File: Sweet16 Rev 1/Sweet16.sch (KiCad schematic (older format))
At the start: 67 parts, among them J1 Conn_01x09_Male, J10 SW_half_inverter, J11 R_clock, J12 OUT_clock, J13 SW_dual8_hex, J14 OUT_OUT, J15 R_sync_pitch_1, J16 SW_sync_1, J17 R_sync_pitch_2, J18 SW_sync_2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

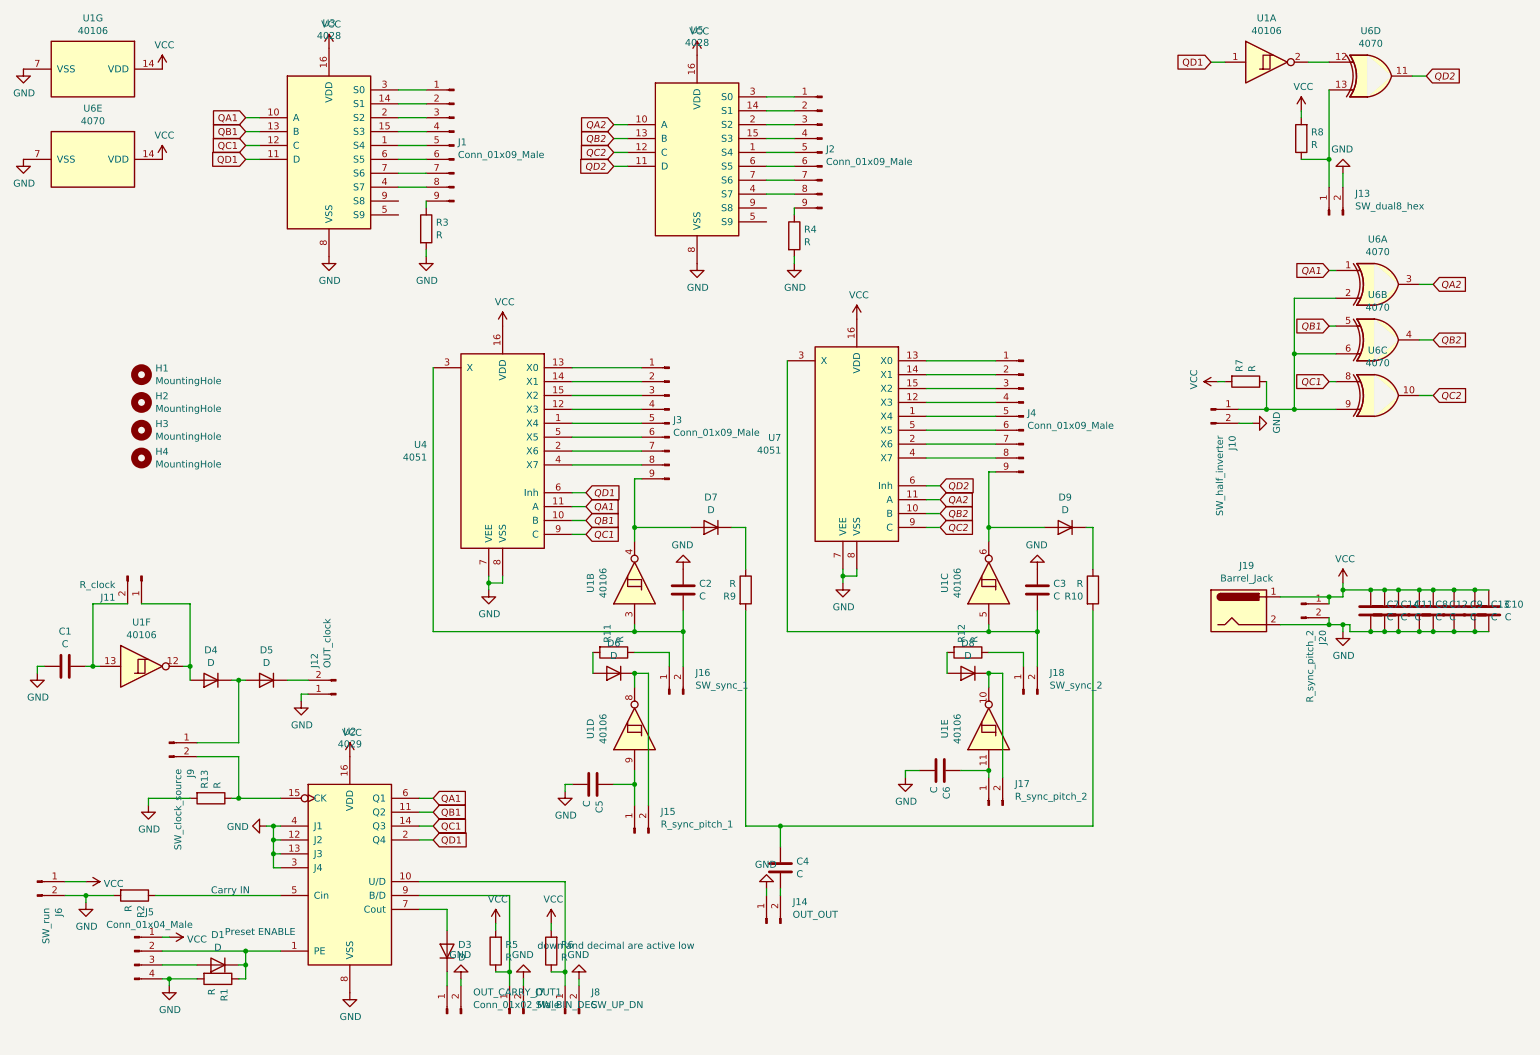
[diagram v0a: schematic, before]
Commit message: moved bits added labels
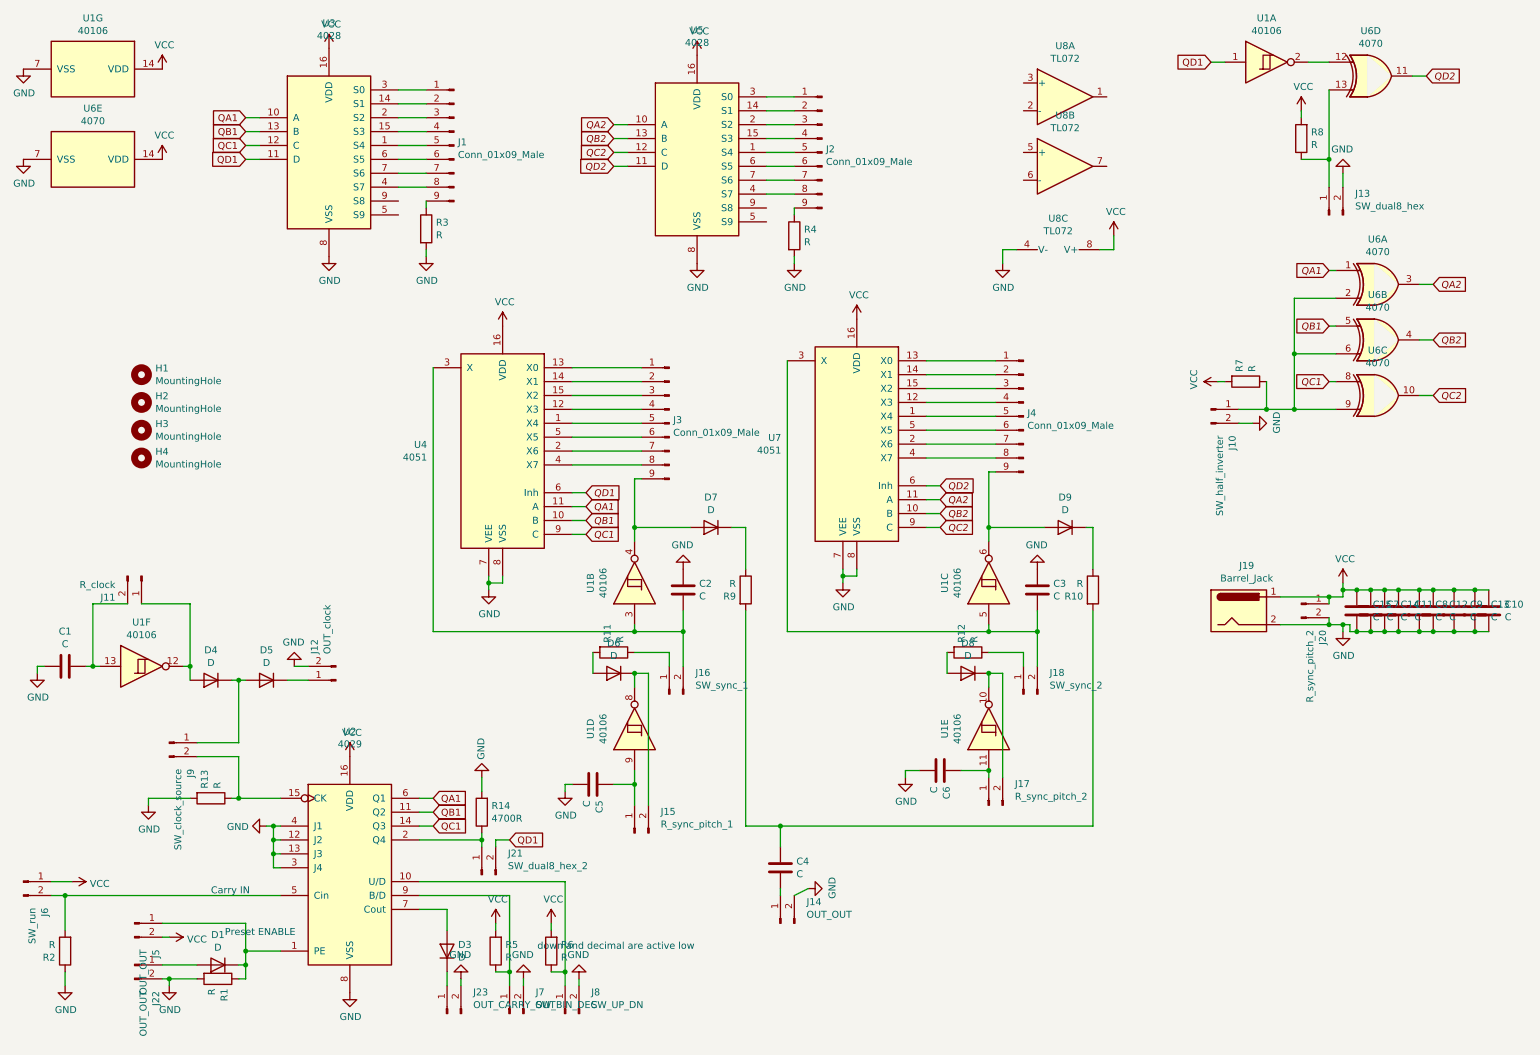
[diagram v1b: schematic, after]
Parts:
- removed J5: Conn_01x04_Male, Connector_PinHeader_2.54mm:PinHeader_1x04_P2.54mm_Vertical, symbol Connector:Conn_01x04_Male
- added C15: C, Capacitor_THT:C_Disc_D6.0mm_W2.5mm_P5.00mm, symbol Device:C
- added J21: SW_dual8_hex_2, Connector_PinHeader_2.54mm:PinHeader_1x02_P2.54mm_Vertical, symbol Connector:Conn_01x02_Male
- added J22, J5: OUT_OUT, Connector_PinHeader_2.54mm:PinHeader_1x02_P2.54mm_Vertical, symbol Connector:Conn_01x02_Male
- added R14: 4700R, Resistor_THT:R_Axial_DIN0207_L6.3mm_D2.5mm_P7.62mm_Horizontal, symbol Device:R
- added U8: TL072, Package_DIP:DIP-8_W7.62mm_LongPads, symbol Amplifier_Operational:TL072
- J23: renamed from OUT_CARRY_OUT1; value Conn_01x02_Male -> OUT_CARRY_OUT
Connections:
- net GND: now also J12.2 (Pin_2), J14.2 (Pin_2), R2.1, C15.1, J22.2 (Pin_2), R14.2, U8.4 (V-); no longer J12.1 (Pin_1), J14.1 (Pin_1), J6.2 (Pin_2), R2.2
- net QD1: now also J21.2 (Pin_2); no longer U2.2 (Q4)
- net VCC: now also C15.2, J5.2 (Pin_2), U8.8 (V+)
- net at D1.1 (K), R1.1, U2.1 (PE): now also J5.1 (Pin_1)
- net at U2.5 (Cin): now also J6.2 (Pin_2), R2.2; no longer R2.1
- net at D1.2 (A): now also J22.1 (Pin_1)
- net at D5.1 (K): now also J12.1 (Pin_1); no longer J12.2 (Pin_2)
- net at C4.1: now also J14.1 (Pin_1); no longer J14.2 (Pin_2)
- new net: J21.1 (Pin_1), R14.1, U2.2 (Q4)
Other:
- moved on the sheet: J12, J14, J6, R2

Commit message: labels
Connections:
- net at D6.1 (K), U1.8: now also J15.1 (Pin_1); no longer J15.2 (Pin_2)
- net at C5.2, U1.9: now also J15.2 (Pin_2); no longer J15.1 (Pin_1)
- net at D8.1 (K), U1.10: now also J17.1 (Pin_1); no longer J17.2 (Pin_2)
- net at C6.2, U1.11: now also J17.2 (Pin_2); no longer J17.1 (Pin_1)
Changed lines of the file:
@@
 L Connector:Conn_01x02_Male J15
 U 1 1 5FCE153F
-P 5000 6400
-F 0 "J15" V 5154 6212 50  0000 R CNN
-F 1 "R_sync_pitch_1" V 5063 6212 50  0000 R CNN
-F 2 "Connector_PinHeader_2.54mm:PinHeader_1x02_P2.54mm_Vertical" H 5000 6400 50  0001 C CNN
-F 3 "~" H 5000 6400 50  0001 C CNN
-	1    5000 6400
-	0    -1   -1   0
+P 5100 6400
+F 0 "J15" V 5254 6212 50  0000 R CNN
+F 1 "R_sync_pitch_1" V 5163 6212 50  0000 R CNN
+F 2 "Connector_PinHeader_2.54mm:PinHeader_1x02_P2.54mm_Vertical" H 5100 6400 50  0001 C CNN
+F 3 "~" H 5100 6400 50  0001 C CNN
+	1    5100 6400
+	0    1    -1   0
 $EndComp
 $Comp
@@
 L Connector:Conn_01x02_Male J17
 U 1 1 5FCDFDEC
-P 7550 6200
-F 0 "J17" V 7704 6012 50  0000 R CNN
-F 1 "R_sync_pitch_2" V 7613 6012 50  0000 R CNN
-F 2 "Connector_PinHeader_2.54mm:PinHeader_1x02_P2.54mm_Vertical" H 7550 6200 50  0001 C CNN
-F 3 "~" H 7550 6200 50  0001 C CNN
-	1    7550 6200
-	0    -1   -1   0
+P 7650 6200
+F 0 "J17" V 7804 6012 50  0000 R CNN
+F 1 "R_sync_pitch_2" V 7713 6012 50  0000 R CNN
+F 2 "Connector_PinHeader_2.54mm:PinHeader_1x02_P2.54mm_Vertical" H 7650 6200 50  0001 C CNN
+F 3 "~" H 7650 6200 50  0001 C CNN
+	1    7650 6200
+	0    1    -1   0
 $EndComp
 $Comp
@@
 	10200 4650 10100 4650
 $Comp
-L power:GND #PWR?
+L power:GND #PWR0142
 U 1 1 6154B30B
 P 7650 2300
-F 0 "#PWR?" H 7650 2050 50  0001 C CNN
+F 0 "#PWR0142" H 7650 2050 50  0001 C CNN
 F 1 "GND" H 7655 2127 50  0000 C CNN
 F 2 "" H 7650 2300 50  0001 C CNN
@@
 $EndComp
 $Comp
-L power:VCC #PWR?
+L power:VCC #PWR0143
 U 1 1 6154BF9B
 P 8450 2100
-F 0 "#PWR?" H 8450 1950 50  0001 C CNN
+F 0 "#PWR0143" H 8450 1950 50  0001 C CNN
 F 1 "VCC" H 8465 2273 50  0000 C CNN
 F 2 "" H 8450 2100 50  0001 C CNN

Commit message: 48 wires to go
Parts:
- removed D7, D9: D, Diode_THT:D_A-405_P7.62mm_Horizontal, symbol Device:D
- removed J19: Barrel_Jack, Connector_BarrelJack:BarrelJack_CUI_PJ-102AH_Horizontal, symbol Connector:Barrel_Jack
- removed R10, R9: R, Resistor_THT:R_Axial_DIN0207_L6.3mm_D2.5mm_P7.62mm_Horizontal, symbol Device:R
- removed U8: TL072, Package_DIP:DIP-8_W7.62mm_LongPads, symbol Amplifier_Operational:TL072
- added R15, R16: 100k, Resistor_THT:R_Axial_DIN0207_L6.3mm_D2.5mm_P7.62mm_Horizontal, symbol Device:R
- added U8: LM358, Package_DIP:DIP-8_W7.62mm_LongPads, symbol Amplifier_Operational:LM358
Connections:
- net GND: now also U8.4 (V-)
- net VCC: now also U8.8 (V+)
- net at J3.9 (Pin_9), U1.4: now also U8.5 (+)
- net at J4.9 (Pin_9), U1.6: now also U8.3 (+)
- net at C4.2: now also R15.1, R16.2
- new net: R16.1, U8.1, U8.2 (-)
- new net: R15.2, U8.6 (-), U8.7
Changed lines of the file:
@@
 	7550 4200 7550 4300
-$Comp
-L Device:R R9
-U 1 1 600316E2
-P 5800 4650
-F 0 "R9" H 5730 4604 50  0000 R CNN
-F 1 "R" H 5730 4695 50  0000 R CNN
-F 2 "Resistor_THT:R_Axial_DIN0207_L6.3mm_D2.5mm_P7.62mm_Horizontal" V 5730 4650 50  0001 C CNN
-F 3 "~" H 5800 4650 50  0001 C CNN
-	1    5800 4650
-	1    0    0    -1
-$EndComp
 $Comp
 L Connector:Conn_01x02_Male J10
@@
 	9550 3350 9750 3350
 $Comp
-L Device:R R10
-U 1 1 60329897
-P 8300 4650
-F 0 "R10" H 8230 4604 50  0000 R CNN
-F 1 "R" H 8230 4695 50  0000 R CNN
-F 2 "Resistor_THT:R_Axial_DIN0207_L6.3mm_D2.5mm_P7.62mm_Horizontal" V 8230 4650 50  0001 C CNN
-F 3 "~" H 8300 4650 50  0001 C CNN
-	1    8300 4650
-	1    0    0    -1
-$EndComp
-Wire Wire Line
-	5800 4800 5800 6350
-Wire Wire Line
-	8300 6350 8300 4800
-Wire Wire Line
-	5800 4200 5800 4500
-Wire Wire Line
-	8300 4200 8300 4500
-$Comp
 L Device:C C4
 U 1 1 603E27DA
@@
 $EndComp
 $Comp
-L Device:D D9
-U 1 1 5FD09EF1
-P 8100 4200
-F 0 "D9" H 8100 3983 50  0000 C CNN
-F 1 "D" H 8100 4074 50  0000 C CNN
-F 2 "Diode_THT:D_A-405_P7.62mm_Horizontal" H 8100 4200 50  0001 C CNN
-F 3 "~" H 8100 4200 50  0001 C CNN
-	1    8100 4200
-	-1   0    0    1
-$EndComp
-$Comp
-L Device:D D7
-U 1 1 5FD0D58A
-P 5550 4200
-F 0 "D7" H 5550 3983 50  0000 C CNN
-F 1 "D" H 5550 4074 50  0000 C CNN
-F 2 "Diode_THT:D_A-405_P7.62mm_Horizontal" H 5550 4200 50  0001 C CNN
-F 3 "~" H 5550 4200 50  0001 C CNN
-	1    5550 4200
-	-1   0    0    1
-$EndComp
-Wire Wire Line
-	5700 4200 5800 4200
-Wire Wire Line
-	8300 4200 8250 4200
-$Comp
 L Device:D D6
 U 1 1 5FD3EE69
@@
 	-1   0    0    1
 $EndComp
-Wire Wire Line
-	6050 6350 8300 6350
-Connection ~ 6050 6350
-Wire Wire Line
-	6050 6350 6050 6500
-Wire Wire Line
-	5800 6350 6050 6350
 $Comp
 L Connector:Conn_01x02_Male J14
@@
 $EndComp
 $Comp
-L Connector:Barrel_Jack J19
-U 1 1 600C4E4A
-P 9350 4800
-F 0 "J19" H 9407 5125 50  0000 C CNN
-F 1 "Barrel_Jack" H 9407 5034 50  0000 C CNN
-F 2 "Connector_BarrelJack:BarrelJack_CUI_PJ-102AH_Horizontal" H 9400 4760 50  0001 C CNN
-F 3 "~" H 9400 4760 50  0001 C CNN
-	1    9350 4800
-	1    0    0    -1
-$EndComp
-$Comp
 L Connector:Conn_01x02_Male J20
 U 1 1 600C58B1
@@
 $EndComp
 Wire Wire Line
-	9650 4700 10000 4700
-Wire Wire Line
 	10100 4700 10100 4650
 Wire Wire Line
@@
 	10100 4650 10100 4600
 Wire Wire Line
-	9650 4900 10000 4900
-Wire Wire Line
 	10100 4900 10100 4950
 Wire Wire Line
@@
 Wire Wire Line
 	10000 4850 10000 4900
-Connection ~ 10000 4900
 Wire Wire Line
 	10000 4900 10100 4900
 Wire Wire Line
 	10000 4750 10000 4700
-Connection ~ 10000 4700
 Wire Wire Line
 	10000 4700 10100 4700
@@
 Wire Wire Line
 	10400 4650 10500 4650
-Wire Wire Line
-	5000 4200 5400 4200
 $Comp
 L power:GND #PWR0138
@@
 	-1   0    0    1
 $EndComp
-Wire Wire Line
-	7550 4200 7950 4200
 $Comp
 L power:GND #PWR0139
@@
 	1600 7050 2200 7050
 $Comp
-L Amplifier_Operational:TL072 U8
-U 1 1 61535B29
-P 8100 1100
-F 0 "U8" H 8100 1467 50  0000 C CNN
-F 1 "TL072" H 8100 1376 50  0000 C CNN
-F 2 "Package_DIP:DIP-8_W7.62mm_LongPads" H 8100 1100 50  0001 C CNN
-F 3 "http://www.ti.com/lit/ds/symlink/tl071.pdf" H 8100 1100 50  0001 C CNN
-	1    8100 1100
-	1    0    0    -1
-$EndComp
-$Comp
-L Amplifier_Operational:TL072 U8
-U 2 1 61536DC3
-P 8100 1600
-F 0 "U8" H 8100 1967 50  0000 C CNN
-F 1 "TL072" H 8100 1876 50  0000 C CNN
-F 2 "Package_DIP:DIP-8_W7.62mm_LongPads" H 8100 1600 50  0001 C CNN
-F 3 "http://www.ti.com/lit/ds/symlink/tl071.pdf" H 8100 1600 50  0001 C CNN
-	2    8100 1600
-	1    0    0    -1
-$EndComp
-$Comp
-L Amplifier_Operational:TL072 U8
-U 3 1 6153A199
-P 8050 2300
-F 0 "U8" V 7725 2300 50  0000 C CNN
-F 1 "TL072" V 7816 2300 50  0000 C CNN
-F 2 "Package_DIP:DIP-8_W7.62mm_LongPads" H 8050 2300 50  0001 C CNN
-F 3 "http://www.ti.com/lit/ds/symlink/tl071.pdf" H 8050 2300 50  0001 C CNN
-	3    8050 2300
-	0    1    1    0
-$EndComp
-$Comp
 L Device:C C15
 U 1 1 6153CD4F
@@
 L power:GND #PWR0142
 U 1 1 6154B30B
-P 7650 2300
-F 0 "#PWR0142" H 7650 2050 50  0001 C CNN
-F 1 "GND" H 7655 2127 50  0000 C CNN
-F 2 "" H 7650 2300 50  0001 C CNN
-F 3 "" H 7650 2300 50  0001 C CNN
-	1    7650 2300
+P 9750 6150
+F 0 "#PWR0142" H 9750 5900 50  0001 C CNN
+F 1 "GND" H 9755 5977 50  0000 C CNN
+F 2 "" H 9750 6150 50  0001 C CNN
+F 3 "" H 9750 6150 50  0001 C CNN
+	1    9750 6150
 	1    0    0    -1
 $EndComp
@@
 L power:VCC #PWR0143
 U 1 1 6154BF9B
-P 8450 2100
-F 0 "#PWR0143" H 8450 1950 50  0001 C CNN
-F 1 "VCC" H 8465 2273 50  0000 C CNN
-F 2 "" H 8450 2100 50  0001 C CNN
-F 3 "" H 8450 2100 50  0001 C CNN
-	1    8450 2100
-	1    0    0    -1
-$EndComp
-Wire Wire Line
-	8350 2200 8450 2200
-Wire Wire Line
-	8450 2200 8450 2100
-Wire Wire Line
-	7750 2200 7650 2200
-Wire Wire Line
-	7650 2200 7650 2300
+P 10550 5950
+F 0 "#PWR0143" H 10550 5800 50  0001 C CNN
+F 1 "VCC" H 10565 6123 50  0000 C CNN
+F 2 "" H 10550 5950 50  0001 C CNN
+F 3 "" H 10550 5950 50  0001 C CNN
+	1    10550 5950
+	1    0    0    -1
+$EndComp
+Wire Wire Line
+	10450 6050 10550 6050
+Wire Wire Line
+	10550 6050 10550 5950
+Wire Wire Line
+	9850 6050 9750 6050
+Wire Wire Line
+	9750 6050 9750 6150
+Wire Wire Line
+	5600 5550 5450 5550
+Wire Wire Line
+	5450 5550 5450 6150
+Wire Wire Line
+	5450 6150 5550 6150
+Wire Wire Line
+	8100 5550 8100 5600
+Wire Wire Line
+	8100 5550 7950 5550
+Wire Wire Line
+	7950 5550 7950 6200
+Wire Wire Line
+	7950 6200 8050 6200
+$Comp
+L Amplifier_Operational:LM358 U8
+U 1 1 6112DB96
+P 8200 5900
+F 0 "U8" V 8154 6130 50  0000 L CNN
+F 1 "LM358" V 8245 6130 50  0000 L CNN
+F 2 "Package_DIP:DIP-8_W7.62mm_LongPads" H 8200 5900 50  0001 C CNN
+F 3 "http://www.ti.com/lit/ds/symlink/lm2904-n.pdf" H 8200 5900 50  0001 C CNN
+	1    8200 5900
+	0    1    1    0
+$EndComp
+$Comp
+L Amplifier_Operational:LM358 U8
+U 2 1 61132740
+P 5700 5850
+F 0 "U8" V 5654 6080 50  0000 L CNN
+F 1 "LM358" V 5745 6080 50  0000 L CNN
+F 2 "Package_DIP:DIP-8_W7.62mm_LongPads" H 5700 5850 50  0001 C CNN
+F 3 "http://www.ti.com/lit/ds/symlink/lm2904-n.pdf" H 5700 5850 50  0001 C CNN
+	2    5700 5850
+	0    1    1    0
+$EndComp
+$Comp
+L Amplifier_Operational:LM358 U8
+U 3 1 61137CD1
+P 10150 6150
+F 0 "U8" V 9825 6150 50  0000 C CNN
+F 1 "LM358" V 9916 6150 50  0000 C CNN
+F 2 "Package_DIP:DIP-8_W7.62mm_LongPads" H 10150 6150 50  0001 C CNN
+F 3 "http://www.ti.com/lit/ds/symlink/lm2904-n.pdf" H 10150 6150 50  0001 C CNN
+	3    10150 6150
+	0    1    1    0
+$EndComp
+$Comp
+L Device:R R15
+U 1 1 6120315D
+P 5850 6400
+F 0 "R15" H 5780 6354 50  0000 R CNN
+F 1 "100k" H 5780 6445 50  0000 R CNN
+F 2 "Resistor_THT:R_Axial_DIN0207_L6.3mm_D2.5mm_P7.62mm_Horizontal" V 5780 6400 50  0001 C CNN
+F 3 "~" H 5850 6400 50  0001 C CNN
+	1    5850 6400
+	0    1    1    0
+$EndComp
+$Comp
+L Device:R R16
+U 1 1 61203A58
+P 6250 6400
+F 0 "R16" H 6180 6354 50  0000 R CNN
+F 1 "100k" H 6180 6445 50  0000 R CNN
+F 2 "Resistor_THT:R_Axial_DIN0207_L6.3mm_D2.5mm_P7.62mm_Horizontal" V 6180 6400 50  0001 C CNN
+F 3 "~" H 6250 6400 50  0001 C CNN
+	1    6250 6400
+	0    1    1    0
+$EndComp
+Wire Wire Line
+	5550 6150 5550 6400
+Wire Wire Line
+	5550 6400 5700 6400
+Connection ~ 5550 6150
+Wire Wire Line
+	5550 6150 5700 6150
+Wire Wire Line
+	6000 6400 6050 6400
+Wire Wire Line
+	6050 6400 6050 6500
+Wire Wire Line
+	6100 6400 6050 6400
+Connection ~ 6050 6400
+Wire Wire Line
+	6400 6400 8050 6400
+Wire Wire Line
+	8050 6400 8050 6200
+Connection ~ 8050 6200
+Wire Wire Line
+	8050 6200 8200 6200
+Wire Wire Line
+	7550 4200 8300 4200
+Wire Wire Line
+	8300 4200 8300 5600
+Wire Wire Line
+	5000 4200 5800 4200
+Wire Wire Line
+	5800 4200 5800 5550
 $EndSCHEMATC

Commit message: routed, but untested
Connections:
- net at C2.1, J16.2 (Pin_2), U4.3 (X): now also U1.5; no longer U1.3
- net at C3.1, J18.2 (Pin_2), U7.3 (X): now also U1.3; no longer U1.5
- net at J3.9 (Pin_9), U8.5 (+): now also U1.6; no longer U1.4
- net at J4.9 (Pin_9), U8.3 (+): now also U1.4; no longer U1.6
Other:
- moved on the sheet: U1B, U1C
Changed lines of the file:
@@
 L 4xxx:40106 U1
 U 2 1 5FBC9159
+P 7550 4600
+F 0 "U1" H 7550 4917 50  0000 C CNN
+F 1 "40106" H 7550 4826 50  0000 C CNN
+F 2 "Package_DIP:DIP-14_W7.62mm_LongPads" H 7550 4600 50  0001 C CNN
+F 3 "https://assets.nexperia.com/documents/data-sheet/HEF40106B.pdf" H 7550 4600 50  0001 C CNN
+	2    7550 4600
+	0    -1   -1   0
+$EndComp
+$Comp
+L 4xxx:40106 U1
+U 3 1 5FBCA510
 P 5000 4600
 F 0 "U1" H 5000 4917 50  0000 C CNN
@@
 F 2 "Package_DIP:DIP-14_W7.62mm_LongPads" H 5000 4600 50  0001 C CNN
 F 3 "https://assets.nexperia.com/documents/data-sheet/HEF40106B.pdf" H 5000 4600 50  0001 C CNN
-	2    5000 4600
+	3    5000 4600
 	0    -1   -1   0
 $EndComp
-$Comp
-L 4xxx:40106 U1
-U 3 1 5FBCA510
-P 7550 4600
-F 0 "U1" H 7550 4917 50  0000 C CNN
-F 1 "40106" H 7550 4826 50  0000 C CNN
-F 2 "Package_DIP:DIP-14_W7.62mm_LongPads" H 7550 4600 50  0001 C CNN
-F 3 "https://assets.nexperia.com/documents/data-sheet/HEF40106B.pdf" H 7550 4600 50  0001 C CNN
-	3    7550 4600
-	0    -1   -1   0
-$EndComp

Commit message: probably done
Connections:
- net QD0: now reaches J21.1 (Pin_1), R14.1, U2.2 (Q4)
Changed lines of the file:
@@
 Wire Wire Line
 	5800 4200 5800 5550
+Text GLabel 3600 6450 3    50   Input ~ 0
+QD0
 $EndSCHEMATC
